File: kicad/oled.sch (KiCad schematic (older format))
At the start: 12 parts, among them Q1 FDN335N, Q2 FDN338P, U2 QG-2864KSWEG01

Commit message: PCB-Platzierung, 3D-Knöpfe, Schaltung wird noch getestet
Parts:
- removed Q1: FDN335N, Package_TO_SOT_SMD:SOT-23, symbol Device:Q_NMOS_GSD
- removed Q2: FDN338P, Package_TO_SOT_SMD:SOT-23, symbol Device:Q_PMOS_GSD
- removed R1, R2: 47k, Resistor_SMD:R_0603_1608Metric, symbol Device:R
- added C5: 1u, Capacitor_SMD:C_0603_1608Metric, symbol Device:C
- added D1: 1N4148, Package_TO_SOT_SMD:SOT-23, symbol Device:D
- added R12, R14, R15, R16: 4k7, Resistor_SMD:R_0603_1608Metric, symbol Device:R
- added R13: 10k, Resistor_SMD:R_0603_1608Metric, symbol Device:R
- C10: renamed from C5; footprint Capacitor_SMD:C_0603_1608Metric -> Capacitor_SMD:C_0805_2012Metric
- C11: renamed from C6; footprint Capacitor_SMD:C_0603_1608Metric -> Capacitor_SMD:C_0805_2012Metric
- U4: renamed from U2; footprint (none) -> gamearino:OLED_128x64_FlatRibbon_30
- renumbered C2 to C6, C1 to C7, C3 to C8, C4 to C9, R3 to R17
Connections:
- net labels added: +3.3V, GNDD
- net labels removed: GND, GPIO, VBAT, VDD, VIN, ~Reset
- wire segments 83 -> 100
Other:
- note added: "TODO: Poti für Helligkeit"
- note removed: "1.65~~3.3V"
- note removed: "3.4~~4.2V"
- note removed: "I/O Voltage"
- note removed: "Switchable VBAT for \npower sequencing"
- moved on the sheet: C10, C11, C6, C7, C8, C9, R17, U4

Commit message: Changelog eingeführt, GND statt GNDD
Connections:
- net labels added: GND
- net labels removed: GNDD
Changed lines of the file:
@@
 	4850 3750 4750 3750
 $Comp
-L power:GNDD #PWR023
+L power:GND #PWR023
 U 1 1 602AD0C5
 P 5650 3800
 F 0 "#PWR023" H 5650 3550 50  0001 C CNN
-F 1 "GNDD" H 5654 3645 50  0000 C CNN
+F 1 "GND" H 5654 3645 50  0000 C CNN
 F 2 "" H 5650 3800 50  0001 C CNN
 F 3 "" H 5650 3800 50  0001 C CNN
@@
 $EndComp
 $Comp
-L power:GNDD #PWR020
+L power:GND #PWR020
 U 1 1 602BFE7A
 P 3850 4200
 F 0 "#PWR020" H 3850 3950 50  0001 C CNN
-F 1 "GNDD" H 3854 4045 50  0000 C CNN
+F 1 "GND" H 3854 4045 50  0000 C CNN
 F 2 "" H 3850 4200 50  0001 C CNN
 F 3 "" H 3850 4200 50  0001 C CNN
@@
 $EndComp
 $Comp
-L power:GNDD #PWR024
+L power:GND #PWR024
 U 1 1 602CD129
 P 5650 4900
 F 0 "#PWR024" H 5650 4650 50  0001 C CNN
-F 1 "GNDD" H 5654 4745 50  0000 C CNN
+F 1 "GND" H 5654 4745 50  0000 C CNN
 F 2 "" H 5650 4900 50  0001 C CNN
 F 3 "" H 5650 4900 50  0001 C CNN
@@
 	5900 5000 5850 5000
 $Comp
-L power:GNDD #PWR022
+L power:GND #PWR022
 U 1 1 602D0245
 P 5450 5050
 F 0 "#PWR022" H 5450 4800 50  0001 C CNN
-F 1 "GNDD" H 5454 4895 50  0000 C CNN
+F 1 "GND" H 5454 4895 50  0000 C CNN
 F 2 "" H 5450 5050 50  0001 C CNN
 F 3 "" H 5450 5050 50  0001 C CNN
@@
 	5850 5000 5450 5000
 $Comp
-L power:GNDD #PWR029
+L power:GND #PWR029
 U 1 1 602F6BC4
 P 7950 4400
 F 0 "#PWR029" H 7950 4150 50  0001 C CNN
-F 1 "GNDD" H 7954 4245 50  0000 C CNN
+F 1 "GND" H 7954 4245 50  0000 C CNN
 F 2 "" H 7950 4400 50  0001 C CNN
 F 3 "" H 7950 4400 50  0001 C CNN
@@
 $EndComp
 $Comp
-L power:GNDD #PWR030
+L power:GND #PWR030
 U 1 1 602FD105
 P 8800 4500
 F 0 "#PWR030" H 8800 4250 50  0001 C CNN
-F 1 "GNDD" H 8804 4345 50  0000 C CNN
+F 1 "GND" H 8804 4345 50  0000 C CNN
 F 2 "" H 8800 4500 50  0001 C CNN
 F 3 "" H 8800 4500 50  0001 C CNN
@@
 $EndComp
 $Comp
-L power:GNDD #PWR031
+L power:GND #PWR031
 U 1 1 603039A1
 P 9200 4500
 F 0 "#PWR031" H 9200 4250 50  0001 C CNN
-F 1 "GNDD" H 9204 4345 50  0000 C CNN
+F 1 "GND" H 9204 4345 50  0000 C CNN
 F 2 "" H 9200 4500 50  0001 C CNN
 F 3 "" H 9200 4500 50  0001 C CNN
@@
 $EndComp
 $Comp
-L power:GNDD #PWR026
+L power:GND #PWR026
 U 1 1 6030A2D7
 P 7650 3850
 F 0 "#PWR026" H 7650 3600 50  0001 C CNN
-F 1 "GNDD" H 7650 3750 45  0000 C CNN
+F 1 "GND" H 7650 3750 45  0000 C CNN
 F 2 "" H 7650 3850 50  0001 C CNN
 F 3 "" H 7650 3850 50  0001 C CNN
@@
 $EndComp
 $Comp
-L power:GNDD #PWR027
+L power:GND #PWR027
 U 1 1 60310BCA
 P 7650 4700
 F 0 "#PWR027" H 7650 4450 50  0001 C CNN
-F 1 "GNDD" H 7654 4545 50  0000 C CNN
+F 1 "GND" H 7654 4545 50  0000 C CNN
 F 2 "" H 7650 4700 50  0001 C CNN
 F 3 "" H 7650 4700 50  0001 C CNN
@@
 $EndComp
 $Comp
-L power:GNDD #PWR028
+L power:GND #PWR028
 U 1 1 60317495
 P 7650 5200
 F 0 "#PWR028" H 7650 4950 50  0001 C CNN
-F 1 "GNDD" H 7654 5045 50  0000 C CNN
+F 1 "GND" H 7654 5045 50  0000 C CNN
 F 2 "" H 7650 5200 50  0001 C CNN
 F 3 "" H 7650 5200 50  0001 C CNN
@@
 $EndComp
 $Comp
-L power:GNDD #PWR025
+L power:GND #PWR025
 U 1 1 6035E0AF
 P 5800 5850
 F 0 "#PWR025" H 5800 5600 50  0001 C CNN
-F 1 "GNDD" H 5804 5695 50  0000 C CNN
+F 1 "GND" H 5804 5695 50  0000 C CNN
 F 2 "" H 5800 5850 50  0001 C CNN
 F 3 "" H 5800 5850 50  0001 C CNN
@@
 	4050 5750 4050 5850
 $Comp
-L power:GNDD #PWR021
+L power:GND #PWR021
 U 1 1 603BC6FD
 P 4050 5850
 F 0 "#PWR021" H 4050 5600 50  0001 C CNN
-F 1 "GNDD" H 4054 5695 50  0000 C CNN
+F 1 "GND" H 4054 5695 50  0000 C CNN
 F 2 "" H 4050 5850 50  0001 C CNN
 F 3 "" H 4050 5850 50  0001 C CNN

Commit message: Pinliste und kleinere Verschönerungen, Transistor-Value, ...
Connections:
- wire segments 100 -> 98
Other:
- moved on the sheet: C8, C9
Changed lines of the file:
@@
 U 1 1 5F88C22A
 P 8800 4300
-F 0 "C10" H 8600 4350 50  0000 L CNN
-F 1 "4u7" H 8600 4200 50  0000 L CNN
+F 0 "C10" H 8915 4346 50  0000 L CNN
+F 1 "4u7" H 8915 4255 50  0000 L CNN
 F 2 "Capacitor_SMD:C_0805_2012Metric" H 8838 4150 50  0001 C CNN
 F 3 "~" H 8800 4300 50  0001 C CNN
@@
 U 1 1 5F88DED6
 P 9200 4300
-F 0 "C11" H 9000 4350 50  0000 L CNN
-F 1 "2u2" H 9000 4200 50  0000 L CNN
+F 0 "C11" H 9315 4346 50  0000 L CNN
+F 1 "2u2" H 9315 4255 50  0000 L CNN
 F 2 "Capacitor_SMD:C_0805_2012Metric" H 9238 4150 50  0001 C CNN
 F 3 "~" H 9200 4300 50  0001 C CNN
@@
 U 1 1 5F89CABD
 P 4750 3950
-F 0 "C7" H 4550 4000 50  0000 L CNN
-F 1 "1u" H 4550 3900 50  0000 L CNN
+F 0 "C7" H 4635 3996 50  0000 R CNN
+F 1 "1u" H 4635 3905 50  0000 R CNN
 F 2 "Capacitor_SMD:C_0603_1608Metric" H 4788 3800 50  0001 C CNN
 F 3 "~" H 4750 3950 50  0001 C CNN
@@
 U 1 1 5F89CE46
 P 4350 3950
-F 0 "C6" H 4150 4000 50  0000 L CNN
-F 1 "1u" H 4150 3900 50  0000 L CNN
+F 0 "C6" H 4235 3996 50  0000 R CNN
+F 1 "1u" H 4235 3905 50  0000 R CNN
 F 2 "Capacitor_SMD:C_0603_1608Metric" H 4388 3800 50  0001 C CNN
 F 3 "~" H 4350 3950 50  0001 C CNN
@@
 L Device:C C9
 U 1 1 5F8948EB
-P 5500 4300
-F 0 "C9" H 5300 4350 50  0000 L CNN
-F 1 "1u" H 5350 4200 50  0000 L CNN
-F 2 "Capacitor_SMD:C_0603_1608Metric" H 5538 4150 50  0001 C CNN
-F 3 "~" H 5500 4300 50  0001 C CNN
-	1    5500 4300
+P 5300 4250
+F 0 "C9" H 5185 4296 50  0000 R CNN
+F 1 "1u" H 5185 4205 50  0000 R CNN
+F 2 "Capacitor_SMD:C_0603_1608Metric" H 5338 4100 50  0001 C CNN
+F 3 "~" H 5300 4250 50  0001 C CNN
+	1    5300 4250
 	1    0    0    -1
 $EndComp
@@
 L Device:C C8
 U 1 1 5F89403B
-P 5300 3950
-F 0 "C8" H 5150 4050 50  0000 L CNN
-F 1 "1u" H 5150 3850 50  0000 L CNN
-F 2 "Capacitor_SMD:C_0603_1608Metric" H 5338 3800 50  0001 C CNN
-F 3 "~" H 5300 3950 50  0001 C CNN
-	1    5300 3950
+P 5300 3850
+F 0 "C8" H 5185 3896 50  0000 R CNN
+F 1 "1u" H 5185 3805 50  0000 R CNN
+F 2 "Capacitor_SMD:C_0603_1608Metric" H 5338 3700 50  0001 C CNN
+F 3 "~" H 5300 3850 50  0001 C CNN
+	1    5300 3850
 	1    0    0    -1
 $EndComp
@@
 	5450 3900 5900 3900
 Wire Wire Line
-	5450 4000 5900 4000
+	5300 3700 5450 3700
 Wire Wire Line
-	5300 3800 5450 3800
-Wire Wire Line
-	5450 3800 5450 3900
-Wire Wire Line
-	5300 4100 5450 4100
-Wire Wire Line
-	5450 4100 5450 4000
+	5450 3700 5450 3900
 $Comp
 L Device:R R?
@@
 AR Path="/6029C673" Ref="R?"  Part="1"
 AR Path="/5F8674B3/6029C673" Ref="R15"  Part="1"
-F 0 "R15" V 4120 3796 50  0000 L CNN
-F 1 "4k7" V 4150 3600 50  0000 L CNN
+F 0 "R15" V 4257 3750 50  0000 C CNN
+F 1 "4k7" V 4166 3750 50  0000 C CNN
 F 2 "Resistor_SMD:R_0603_1608Metric" V 3980 3750 50  0001 C CNN
 F 3 "~" H 4050 3750 50  0001 C CNN
@@
 Connection ~ 4750 3750
 Wire Wire Line
-	4850 3750 4750 3750
+	4950 3750 4750 3750
 $Comp
 L power:GND #PWR023
@@
 P 5650 3800
 F 0 "#PWR023" H 5650 3550 50  0001 C CNN
-F 1 "GND" H 5654 3645 50  0000 C CNN
+F 1 "GND" V 5527 3763 50  0000 C CNN
 F 2 "" H 5650 3800 50  0001 C CNN
 F 3 "" H 5650 3800 50  0001 C CNN
 	1    5650 3800
-	1    0    0    -1
+	0    1    1    0
 $EndComp
 $Comp
@@
 	1    0    0    -1
 $EndComp
-$Comp
-L power:GND #PWR024
-U 1 1 602CD129
-P 5650 4900
-F 0 "#PWR024" H 5650 4650 50  0001 C CNN
-F 1 "GND" H 5654 4745 50  0000 C CNN
-F 2 "" H 5650 4900 50  0001 C CNN
-F 3 "" H 5650 4900 50  0001 C CNN
-	1    5650 4900
-	1    0    0    -1
-$EndComp
-Wire Wire Line
-	5900 4900 5650 4900
 Wire Wire Line
 	5900 4700 5850 4700
 Wire Wire Line
-	5850 4700 5850 5000
+	5850 4700 5850 4900
 Wire Wire Line
 	5900 5000 5850 5000
@@
 P 7650 3850
 F 0 "#PWR026" H 7650 3600 50  0001 C CNN
-F 1 "GND" H 7650 3750 45  0000 C CNN
+F 1 "GND" H 7573 3813 45  0000 R CNN
 F 2 "" H 7650 3850 50  0001 C CNN
 F 3 "" H 7650 3850 50  0001 C CNN
@@
 	5900 4600 5800 4600
 Wire Wire Line
-	4850 3750 4850 4600
+	4950 3750 4950 4600
 Wire Wire Line
 	5800 4300 5800 4600
@@
 Connection ~ 5800 4600
 Wire Wire Line
-	5800 4600 4850 4600
+	5800 4600 4950 4600
 Wire Wire Line
 	4350 4200 3850 4200
@@
 	7350 4100 8800 4100
 Wire Wire Line
-	5900 4100 5500 4100
-Wire Wire Line
-	5500 4100 5500 4150
+	5900 4100 5300 4100
 Wire Wire Line
-	5900 4200 5750 4200
+	5900 4200 5450 4200
 Wire Wire Line
-	5750 4200 5750 4450
+	5450 4200 5450 4400
 Wire Wire Line
-	5750 4450 5500 4450
+	5450 4400 5300 4400
 Wire Wire Line
-	5900 4800 5400 4800
+	5900 4800 5200 4800
 Wire Wire Line
 	8000 4900 8000 6100
@@
 U 1 1 603B7FDC
 P 4050 5600
-F 0 "C5" H 3850 5650 50  0000 L CNN
-F 1 "1u" H 3850 5550 50  0000 L CNN
+F 0 "C5" H 4165 5646 50  0000 L CNN
+F 1 "1u" H 4165 5555 50  0000 L CNN
 F 2 "Capacitor_SMD:C_0603_1608Metric" H 4088 5450 50  0001 C CNN
 F 3 "~" H 4050 5600 50  0001 C CNN
@@
 U 1 1 603CB969
 P 3650 5450
-F 0 "R13" V 3765 5450 50  0000 C CNN
-F 1 "10k" V 3856 5450 50  0000 C CNN
+F 0 "R13" V 3443 5450 50  0000 C CNN
+F 1 "10k" V 3534 5450 50  0000 C CNN
 F 2 "Resistor_SMD:R_0603_1608Metric" V 3580 5450 50  0001 C CNN
 F 3 "~" H 3650 5450 50  0001 C CNN
@@
 	3950 5050 3650 5050
 Wire Wire Line
-	4050 5050 5400 5050
+	4050 5050 5200 5050
 Wire Wire Line
-	5400 4800 5400 5050
+	5200 4800 5200 5050
 Connection ~ 4050 5050
 Connection ~ 4050 5450
@@
 	1    0    0    -1
 $EndComp
+Wire Wire Line
+	5900 4900 5850 4900
+Connection ~ 5850 4900
+Wire Wire Line
+	5850 4900 5850 5000
+Wire Wire Line
+	5300 4000 5900 4000
 $EndSCHEMATC

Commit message: Fertiges Layout v0.0.2, 3 Stk bestellt
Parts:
- added C12: 1u, Capacitor_SMD:C_0603_1608Metric, symbol Device:C
- C10: value 4u7 -> 10u/16V/X5R; DistOrderNr (none) -> C1713; Distributor (none) -> LCSC; ManPartNr (none) -> CL21A106KOQNNNE; Manufacturer (none) -> Samsung; Notes (none) -> 10uF ±10% 16V X5R; PriceEUR (none) -> 0.011386; PriceForQty (none) -> 200; Weblink (none) -> https://lcsc.com/product-detail/Multilayer-Ceramic-Capacito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
- C11: value 2u2 -> 1u; footprint Capacitor_SMD:C_0805_2012Metric -> Capacitor_SMD:C_0603_1608Metric; DistOrderNr (none) -> C1592; Distributor (none) -> LCSC; ManPartNr (none) -> CL10A105KO8NNNC; Manufacturer (none) -> Samsung; Notes (none) -> 1uF ±10% 16V X5R; PriceEUR (none) -> 0.0039; PriceForQty (none) -> 500
- C5, C6, C7, C8, C9: DistOrderNr (none) -> C1592; Distributor (none) -> LCSC; ManPartNr (none) -> CL10A105KO8NNNC; Manufacturer (none) -> Samsung; Notes (none) -> 1uF ±10% 16V X5R; PriceEUR (none) -> 0.0039; PriceForQty (none) -> 500
- D1: value 1N4148 -> BAV99; symbol Device:D -> Diode:BAV99; DistOrderNr (none) -> C181111; Distributor (none) -> LCSC; ManPartNr (none) -> BAV99; Manufacturer (none) -> Guangdong Hottech; Notes (none) -> 70V 200mA 1.25V @ 150mA 6ns; PriceEUR (none) -> 0.0097; PriceForQty (none) -> 50; Weblink (none) -> https://lcsc.com/product-detail/Switching-Diode_BAV99-chip0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
- U4: DistOrderNr (none) -> C85007; Distributor (none) -> LCSC; ManPartNr (none) -> QG-2864KSWEG01; Manufacturer (none) -> Shenzhen Allvision Tech
- renumbered R12 to R14, R13 to R15, R14 to R16, R15 to R17, R16 to R18, R17 to R19
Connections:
- wire segments 98 -> 101
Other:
- note added: "C10 war orignal ein 4u7"
- note added: "C11+C12 waren orignal ein einzelner 2u2"

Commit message: BOM fertig eingepflegt
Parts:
- R14, R16, R17, R18: DistOrderNr (none) -> C103662; Distributor (none) -> LCSC; ManPartNr (none) -> RTT03472JTP; Manufacturer (none) -> RALEC; Notes (none) -> 4.7kΩ ±5% 0.1W ±100ppm/K; PriceEUR (none) -> 0.0015; PriceForQty (none) -> 100
- R15: DistOrderNr (none) -> C103210; Distributor (none) -> LCSC; ManPartNr (none) -> RTT03103JTP; Manufacturer (none) -> RALEC; Notes (none) -> 10kΩ ±5% 0.1W ±100ppm/℃; PriceEUR (none) -> 0.0015; PriceForQty (none) -> 100
- R19: DistOrderNr (none) -> C158905; Distributor (none) -> LCSC; ManPartNr (none) -> RTT03914JTP; Manufacturer (none) -> RALEC; Notes (none) -> 910kΩ ±5% 0.1W ±100ppm/℃; PriceEUR (none) -> 0.0015; PriceForQty (none) -> 100
- U4: PriceEUR (none) -> 2.3984; PriceForQty (none) -> 30
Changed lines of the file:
@@
 F 2 "Resistor_SMD:R_0603_1608Metric" V 7630 4200 50  0001 C CNN
 F 3 "~" H 7700 4200 50  0001 C CNN
+F 4 "C158905" H 7700 4200 50  0001 C CNN "DistOrderNr"
+F 5 "LCSC" H 7700 4200 50  0001 C CNN "Distributor"
+F 6 "RTT03914JTP" H 7700 4200 50  0001 C CNN "ManPartNr"
+F 7 "RALEC" H 7700 4200 50  0001 C CNN "Manufacturer"
+F 8 "910kΩ ±5% 0.1W ±100ppm/℃" H 7700 4200 50  0001 C CNN "Notes"
+F 9 "0.0015" H 7700 4200 50  0001 C CNN "PriceEUR"
+F 10 "100" H 7700 4200 50  0001 C CNN "PriceForQty"
 	1    7700 4200
 	0    1    1    0
@@
 F 2 "Resistor_SMD:R_0603_1608Metric" V 3980 3750 50  0001 C CNN
 F 3 "~" H 4050 3750 50  0001 C CNN
+F 4 "C103662" H 4050 3750 50  0001 C CNN "DistOrderNr"
+F 5 "LCSC" H 4050 3750 50  0001 C CNN "Distributor"
+F 6 " RTT03472JTP" H 4050 3750 50  0001 C CNN "ManPartNr"
+F 7 "RALEC" H 4050 3750 50  0001 C CNN "Manufacturer"
+F 8 "4.7kΩ ±5% 0.1W ±100ppm/K" H 4050 3750 50  0001 C CNN "Notes"
+F 9 "0.0015" H 4050 3750 50  0001 C CNN "PriceEUR"
+F 10 "100" H 4050 3750 50  0001 C CNN "PriceForQty"
 	1    4050 3750
 	0    -1   -1   0
@@
 F 2 "Resistor_SMD:R_0603_1608Metric" V 5730 5650 50  0001 C CNN
 F 3 "~" H 5800 5650 50  0001 C CNN
+F 4 "C103662" H 5800 5650 50  0001 C CNN "DistOrderNr"
+F 5 "LCSC" H 5800 5650 50  0001 C CNN "Distributor"
+F 6 " RTT03472JTP" H 5800 5650 50  0001 C CNN "ManPartNr"
+F 7 "RALEC" H 5800 5650 50  0001 C CNN "Manufacturer"
+F 8 "4.7kΩ ±5% 0.1W ±100ppm/K" H 5800 5650 50  0001 C CNN "Notes"
+F 9 "0.0015" H 5800 5650 50  0001 C CNN "PriceEUR"
+F 10 "100" H 5800 5650 50  0001 C CNN "PriceForQty"
 	1    5800 5650
 	1    0    0    -1
@@
 F 2 "Resistor_SMD:R_0603_1608Metric" V 3580 4850 50  0001 C CNN
 F 3 "~" H 3650 4850 50  0001 C CNN
+F 4 "C103662" H 3650 4850 50  0001 C CNN "DistOrderNr"
+F 5 "LCSC" H 3650 4850 50  0001 C CNN "Distributor"
+F 6 " RTT03472JTP" H 3650 4850 50  0001 C CNN "ManPartNr"
+F 7 "RALEC" H 3650 4850 50  0001 C CNN "Manufacturer"
+F 8 "4.7kΩ ±5% 0.1W ±100ppm/K" H 3650 4850 50  0001 C CNN "Notes"
+F 9 "0.0015" H 3650 4850 50  0001 C CNN "PriceEUR"
+F 10 "100" H 3650 4850 50  0001 C CNN "PriceForQty"
 	1    3650 4850
 	1    0    0    -1
@@
 F 2 "Resistor_SMD:R_0603_1608Metric" V 3580 5450 50  0001 C CNN
 F 3 "~" H 3650 5450 50  0001 C CNN
+F 4 "C103210" H 3650 5450 50  0001 C CNN "DistOrderNr"
+F 5 "LCSC" H 3650 5450 50  0001 C CNN "Distributor"
+F 6 "RTT03103JTP" H 3650 5450 50  0001 C CNN "ManPartNr"
+F 7 "RALEC" H 3650 5450 50  0001 C CNN "Manufacturer"
+F 8 "10kΩ ±5% 0.1W ±100ppm/℃" H 3650 5450 50  0001 C CNN "Notes"
+F 9 "0.0015" H 3650 5450 50  0001 C CNN "PriceEUR"
+F 10 "100" H 3650 5450 50  0001 C CNN "PriceForQty"
 	1    3650 5450
 	0    1    1    0
@@
 F 2 "Resistor_SMD:R_0603_1608Metric" V 3880 4850 50  0001 C CNN
 F 3 "~" H 3950 4850 50  0001 C CNN
+F 4 "C103662" H 3950 4850 50  0001 C CNN "DistOrderNr"
+F 5 "LCSC" H 3950 4850 50  0001 C CNN "Distributor"
+F 6 " RTT03472JTP" H 3950 4850 50  0001 C CNN "ManPartNr"
+F 7 "RALEC" H 3950 4850 50  0001 C CNN "Manufacturer"
+F 8 "4.7kΩ ±5% 0.1W ±100ppm/K" H 3950 4850 50  0001 C CNN "Notes"
+F 9 "0.0015" H 3950 4850 50  0001 C CNN "PriceEUR"
+F 10 "100" H 3950 4850 50  0001 C CNN "PriceForQty"
 	1    3950 4850
 	1    0    0    -1
@@
 F 7 "QG-2864KSWEG01" H 6650 4500 50  0001 C CNN "ManPartNr"
 F 8 "Shenzhen Allvision Tech" H 6650 4500 50  0001 C CNN "Manufacturer"
+F 9 "2.3984" H 6650 4500 50  0001 C CNN "PriceEUR"
+F 10 "30" H 6650 4500 50  0001 C CNN "PriceForQty"
 	1    6650 4500
 	1    0    0    -1

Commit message: wip
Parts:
- D1: symbol Diode:BAV99 -> gamearino-rescue:BAV99-Diode
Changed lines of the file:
@@
 Connection ~ 4050 5450
 $Comp
-L Diode:BAV99 D1
+L gamearino-rescue:BAV99-Diode D1
 U 1 1 603B5519
 P 4050 5250

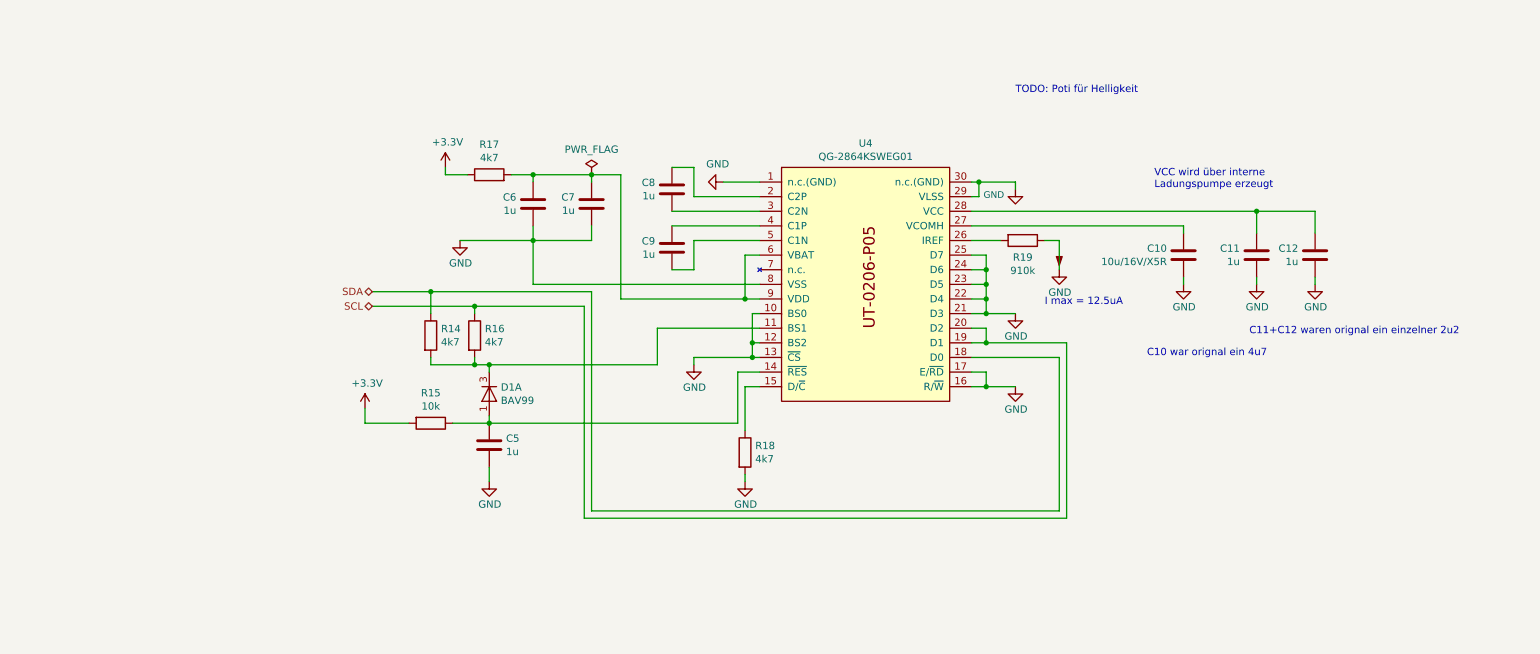
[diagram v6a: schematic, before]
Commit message: Schaltplanänderungen für v20.0.3 eingepflegt
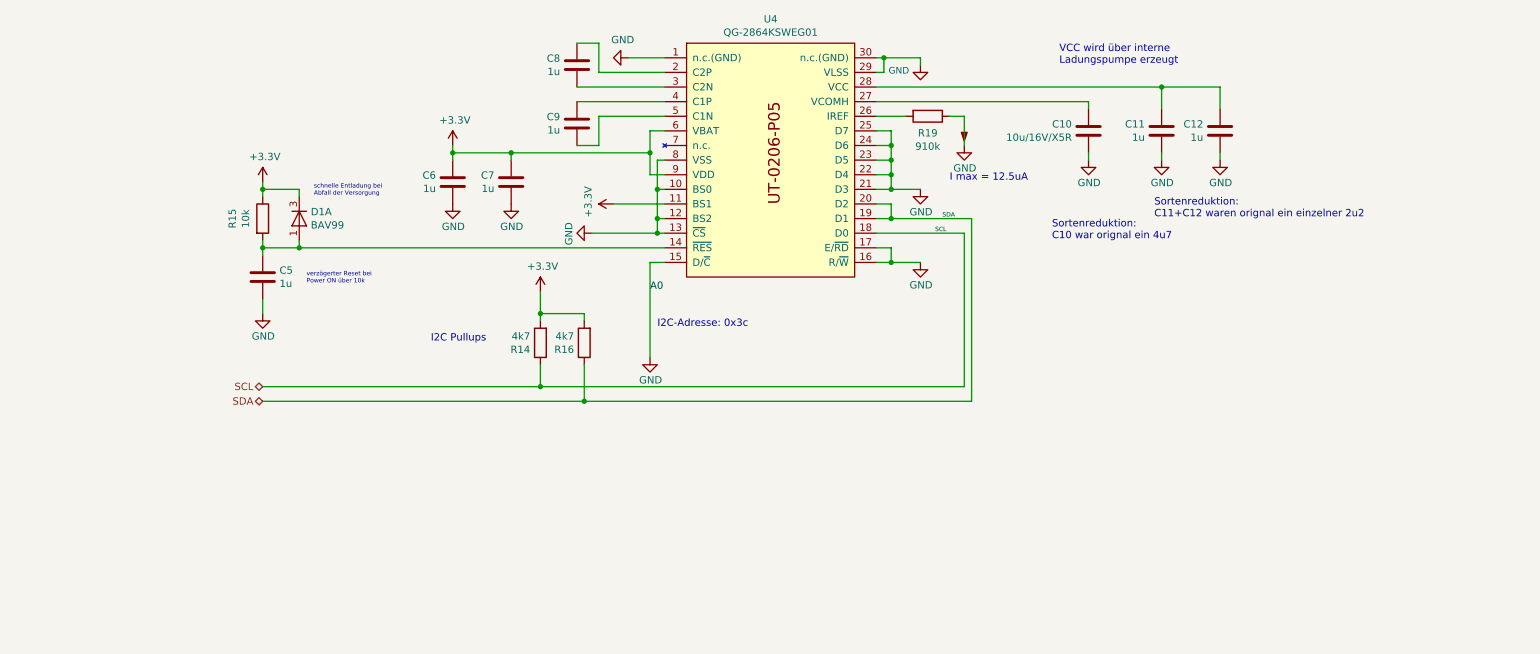
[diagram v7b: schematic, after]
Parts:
- removed R17, R18: 4k7, Resistor_SMD:R_0603_1608Metric, symbol Device:R
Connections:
- net +3V3: now also C6.1, C7.1, D1.3 (K), R14.2, R15.1, R16.2, U4.11 (BS1), U4.6 (VBAT), U4.9 (VDD); no longer R15.2
- net GND: now also U4.15 (D/~C)
- net SCL: now also R14.1, U4.18 (D0); no longer R16.1, U4.19 (D1), U4.20 (D2)
- net SDA: now also R16.1, U4.19 (D1), U4.20 (D2); no longer R14.1, U4.18 (D0)
- net at C5.1, D1.1 (A), U4.14 (~RES): now also R15.2; no longer R15.1
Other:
- note added: "I2C Pullups"
- note added: "I2C-Adresse: 0x3c"
- note added: "Sortenreduktion:\nC10 war orignal ein 4u7"
- note added: "Sortenreduktion:\nC11+C12 waren orignal ein einzelner 2u2"
- note added: "schnelle Entladung bei\nAbfall der Versorgung"
- note added: "verzögerter Reset bei \nPower ON über 10k"
- note removed: "C10 war orignal ein 4u7"
- note removed: "C11+C12 waren orignal ein einzelner 2u2"
- note removed: "TODO: Poti für Helligkeit"
- moved on the sheet: C10, C11, C12, C5, C6, C7, C8, C9, D1A, R14, R15, R16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
